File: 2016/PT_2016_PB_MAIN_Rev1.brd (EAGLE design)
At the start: 150.9 x 201.9 mm, 135 parts, among them Q1 Q_IRFS7437PbF, Q11 Q_IRFS7437PbF, Q12 2N7002, Q14 Q_IRFS7437PbF, Q16 Q_IRFS7437PbF, Q2 2N7002, Q20 Q_IRFS7437PbF, Q6 Q_IRFS7437PbF, Q7 Q_IRFS7437PbF, Q9 Q_IRFS7437PbF

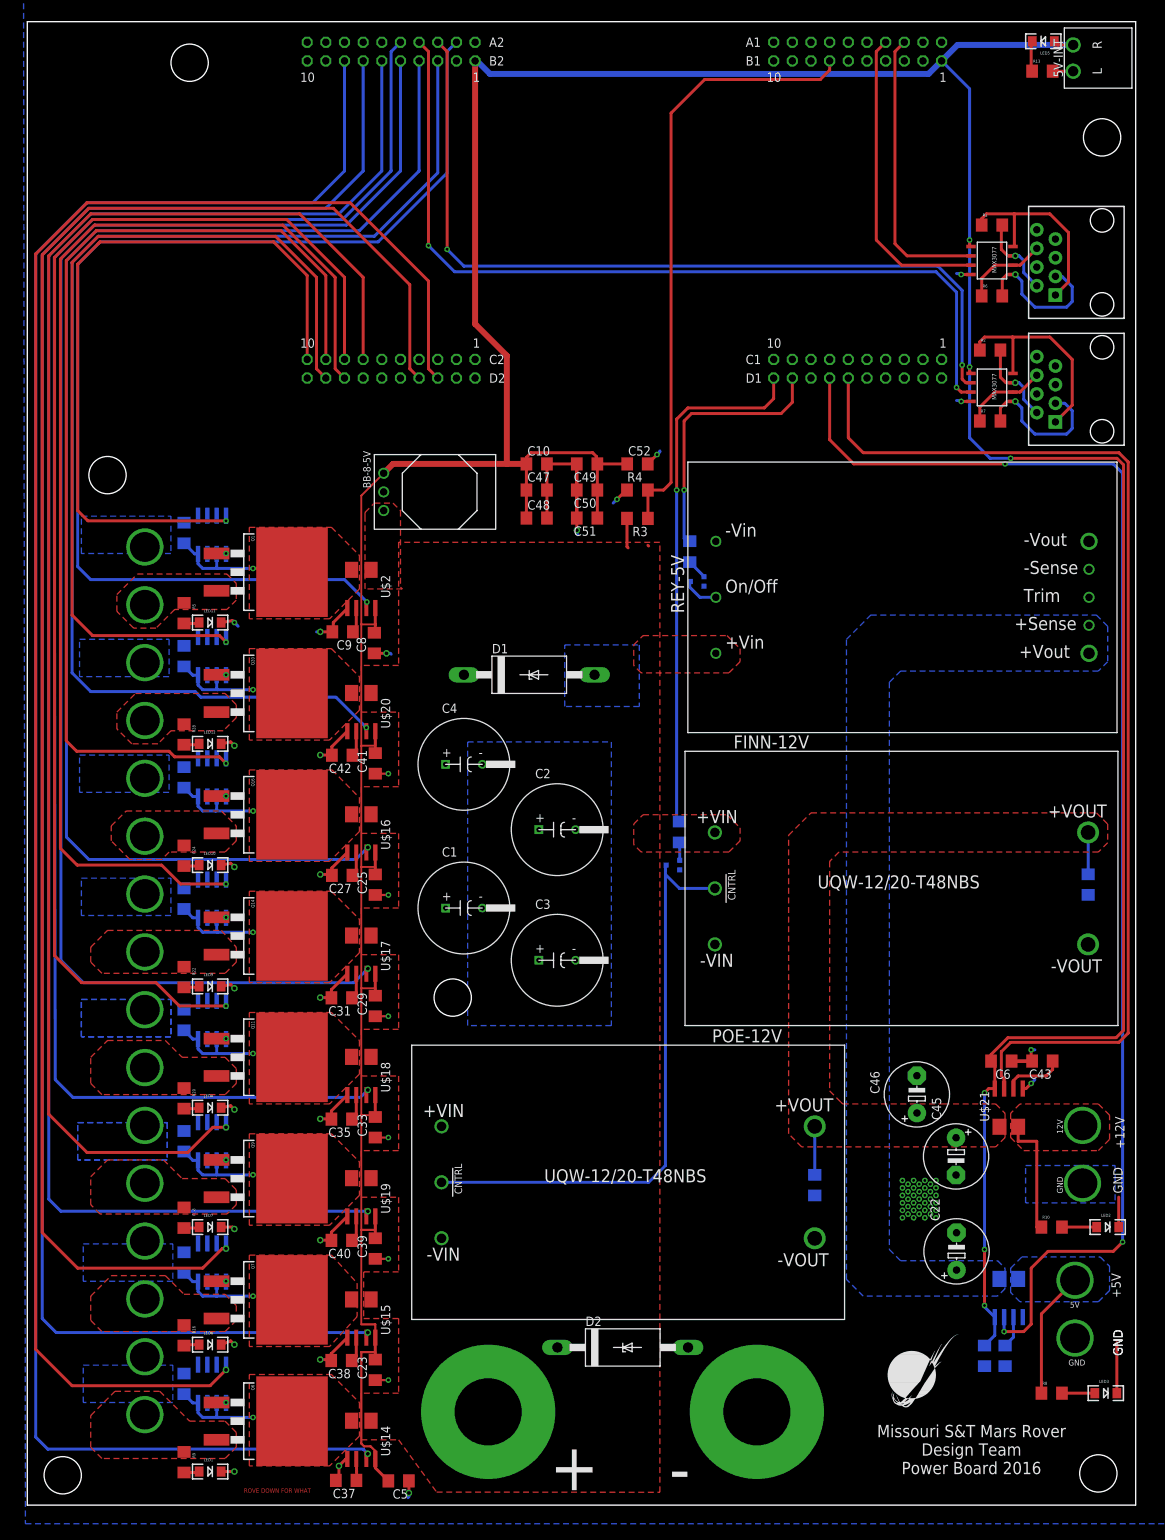
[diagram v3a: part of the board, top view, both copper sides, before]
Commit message: Added mounting wings for APP and rerouted
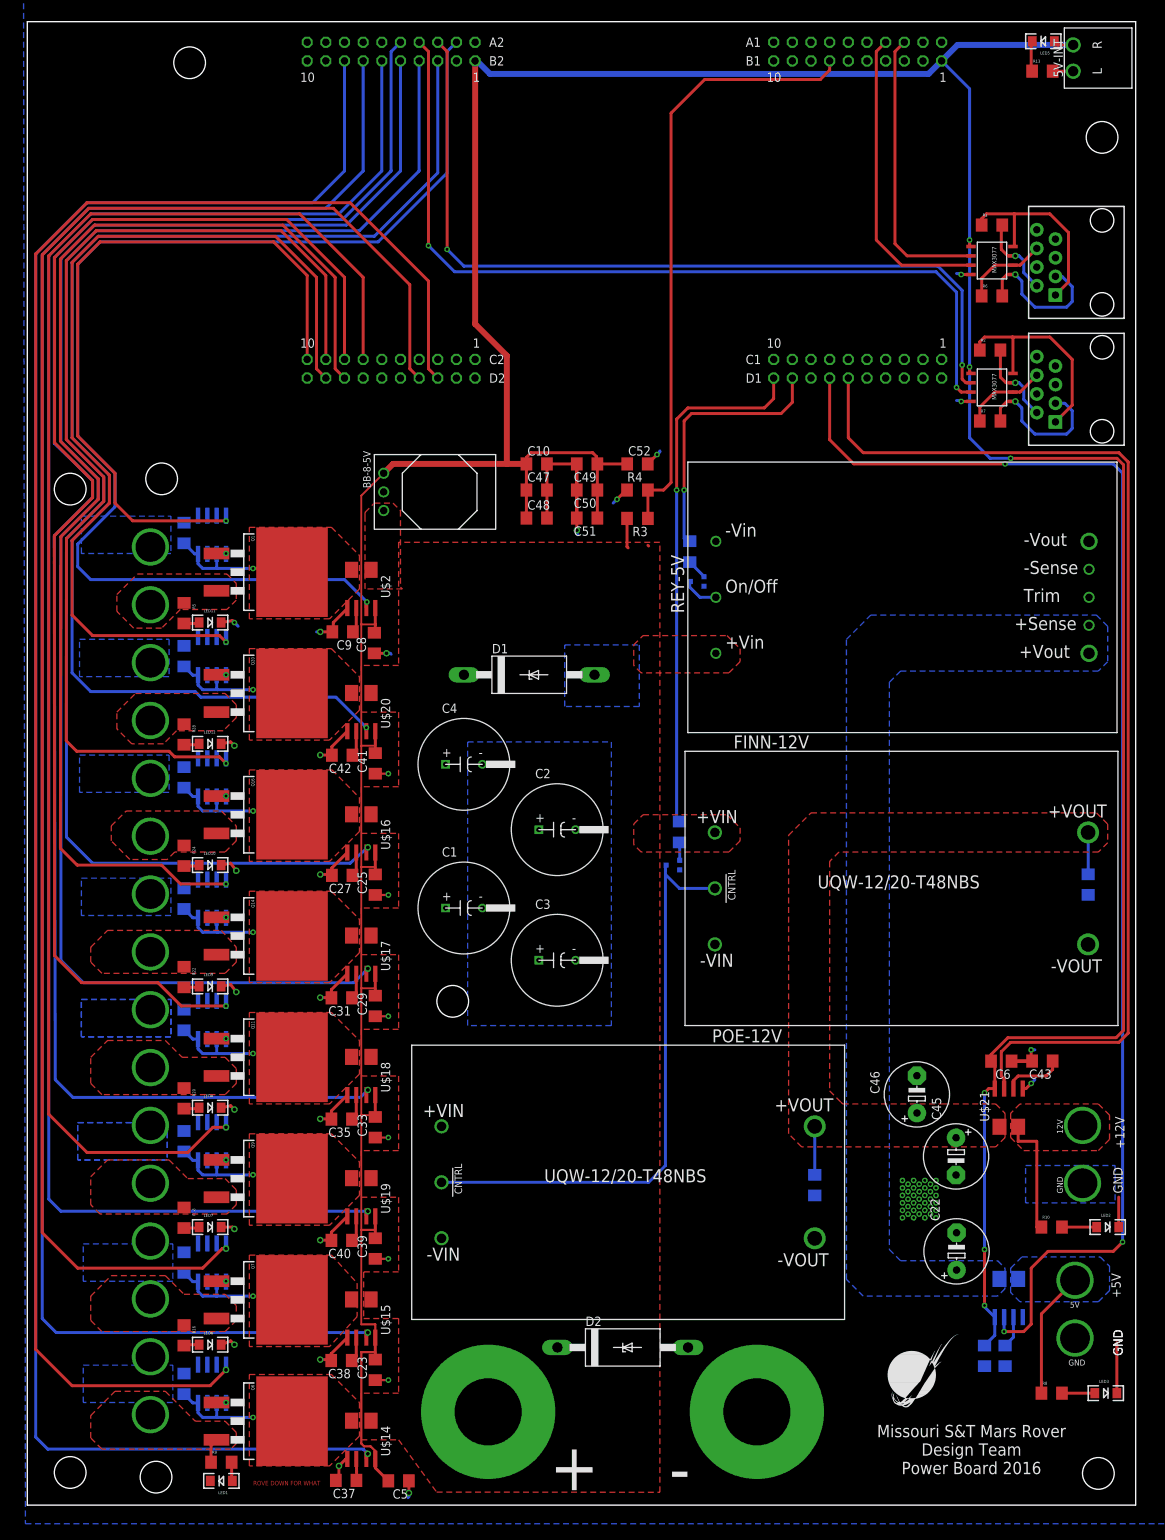
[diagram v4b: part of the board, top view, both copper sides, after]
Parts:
- added U$41, U$42: APP_MOUTING_WINGHORIZ, MRDT-Connectors:PP_MOUNTING_WING_HORIZ
- moved R9 5.08 mm to (21.6, 2.03), turned to 0 degrees
- moved LED1 1.98 mm to (21.6, -0.51), turned to 180 degrees
- moved U$25 0.76 mm to (-16.3, 75.4)
- moved U$26 0.76 mm to (-16.3, 114.8)
- moved U$27 0.76 mm to (-16.3, 43.9)
- moved U$28 0.76 mm to (-16.3, 67.6)
- moved U$29 0.76 mm to (-16.3, 106.9)
- moved U$30 0.76 mm to (-16.3, 99.1)
- moved U$31 0.76 mm to (-16.3, 122.7)
- moved U$32 0.76 mm to (-16.3, 36.1)
- moved U$33 0.76 mm to (-16.3, 91.2)
- moved U$34 0.76 mm to (-16.3, 51.8)
- moved U$35 0.76 mm to (-16.3, 12.4)
- moved U$36 0.76 mm to (-16.3, 83.3)
- moved U$37 0.76 mm to (-16.3, 59.7)
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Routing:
- net M6-IMEAS: track 191.2 -> 195.8 mm
- net M4-IMEAS: track 225.5 -> 229.8 mm
- net M4-SIG: track 177.9 -> 182.2 mm
- net M5-SIG: track 162.0 -> 166.2 mm
- net M6-SIG: track 140.1 -> 144.3 mm
- net AUX_P-IMEAS: track 169.6 -> 173.8 mm
- net M5-IMEAS: track 206.4 -> 210.6 mm
- net AUX_P2-IMEAS: track 157.2 -> 161.4 mm
- net AUX_P-SIG: track 122.5 -> 126.7 mm
- net AUX_P2-SIG: track 100.8 -> 97.3 mm
- net N$41: track 0.00 -> 3.36 mm
- net GND: track 136.9 -> 136.2 mm, vias 70 -> 69

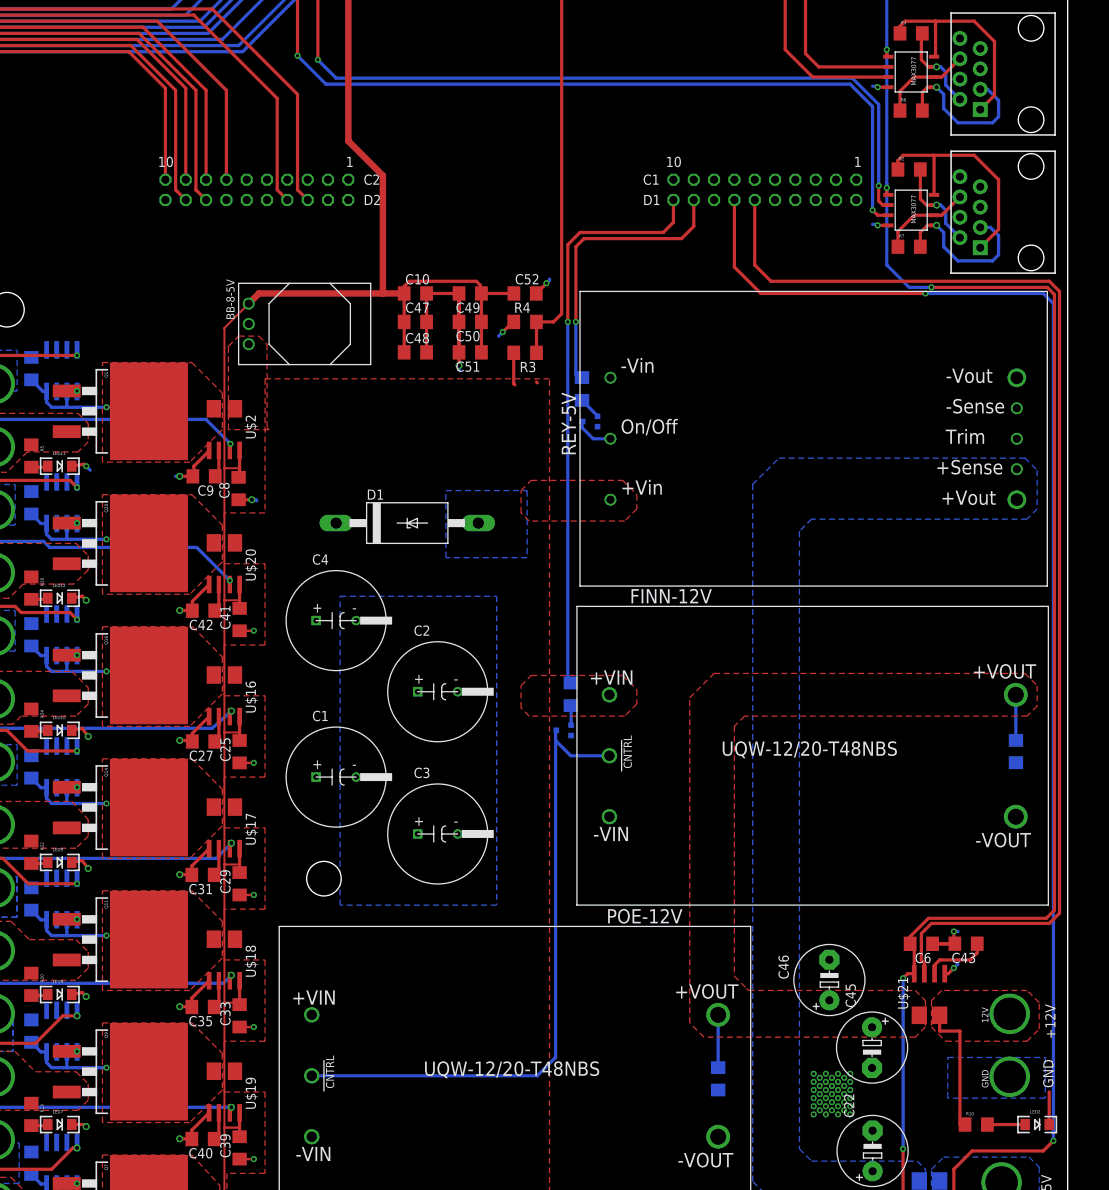
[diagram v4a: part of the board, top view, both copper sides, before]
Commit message: Fixed some clearance issues
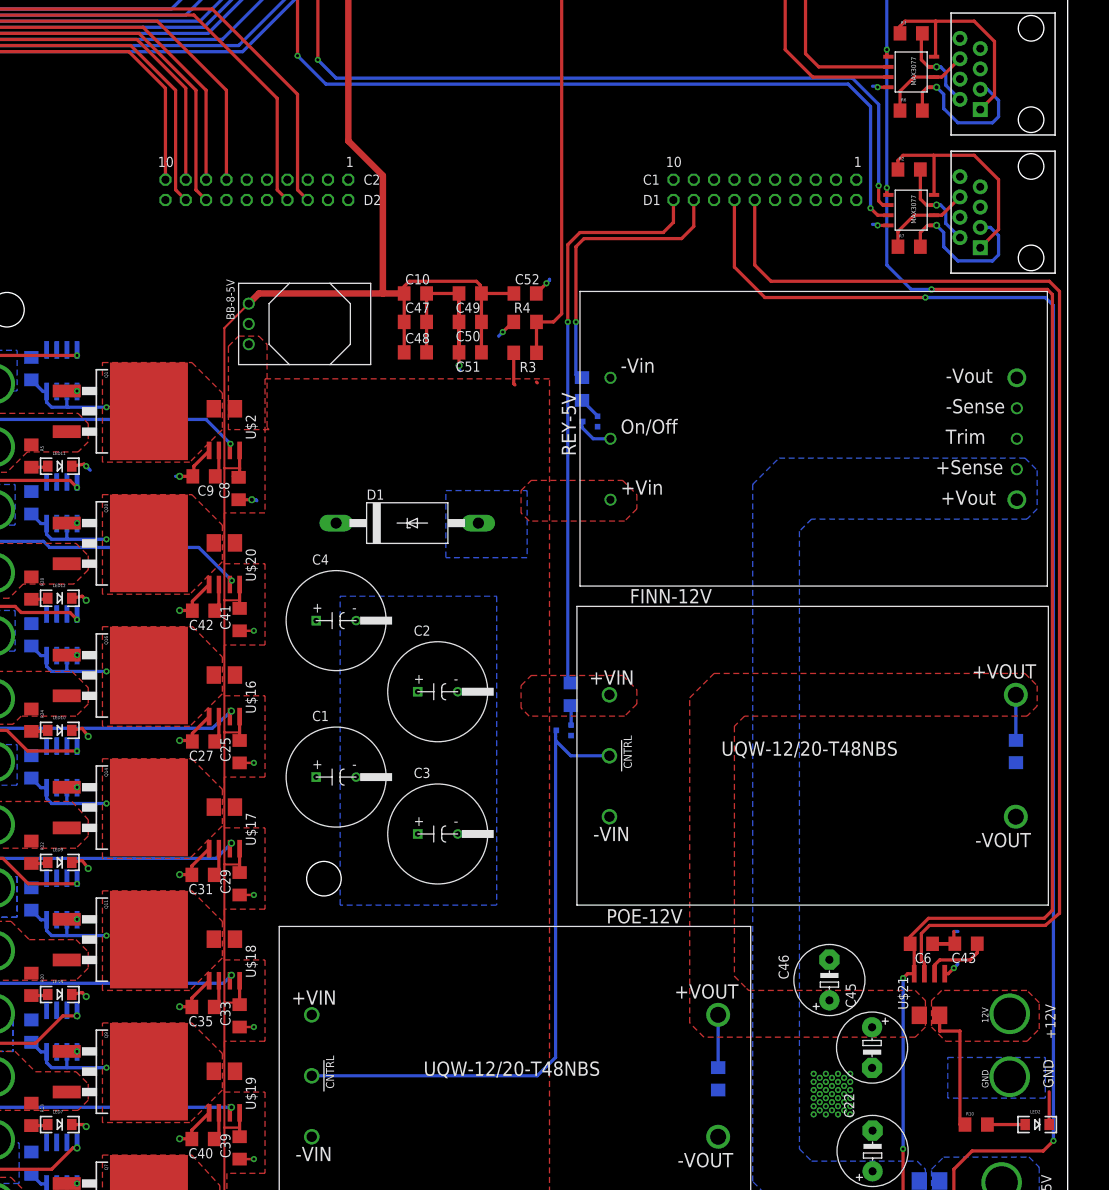
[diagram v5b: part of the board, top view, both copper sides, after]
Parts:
- renumbered U$25 to M5-, U$26 to AUX2+, U$27 to M3-, U$28 to M5+, U$29 to AUX1-, U$30 to AUX1+, U$31 to AUX2-, U$32 to M3+, U$33 to M6-, U$34 to M4+, U$35 to M1-, U$36 to M6+, U$37 to M4-, U$38 to M2+, U$39 to M2-, U$40 to M1+
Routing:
- net +5V: track 592.9 -> 592.4 mm
- net GND: vias 69 -> 68

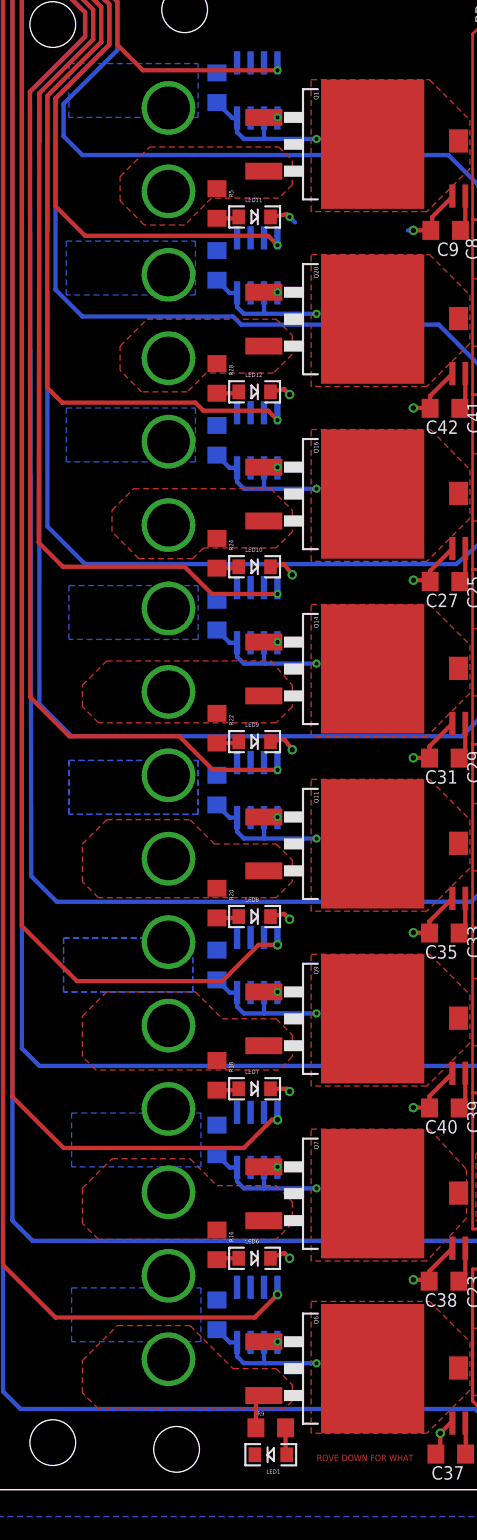
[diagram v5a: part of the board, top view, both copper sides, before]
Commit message: Deleted Unnecessary Polygons
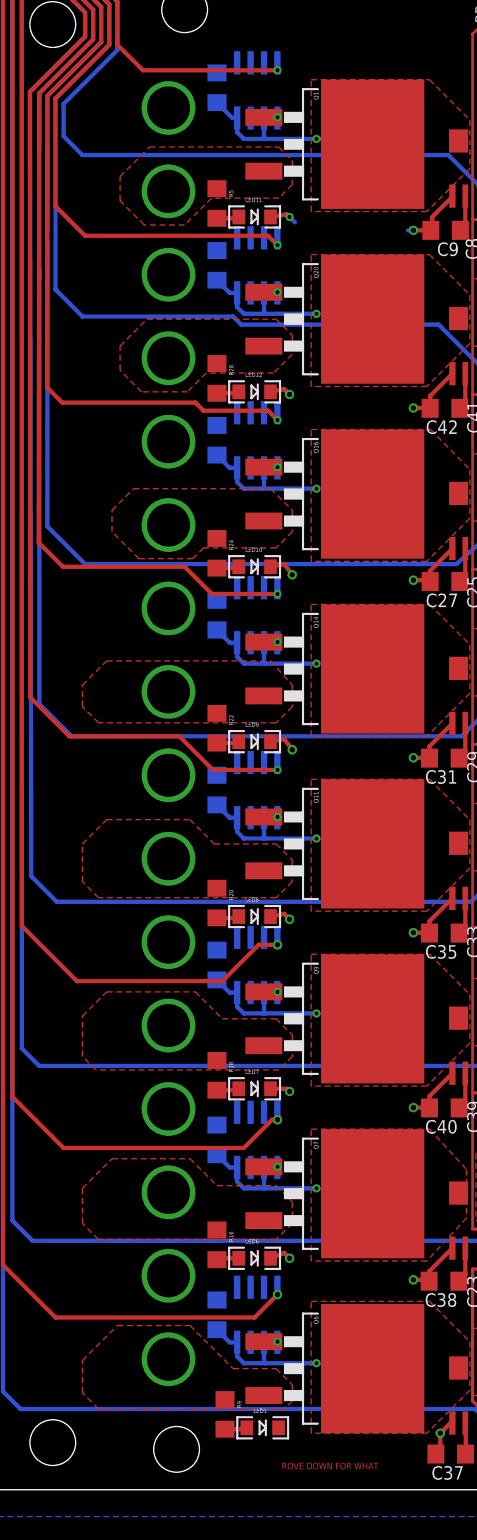
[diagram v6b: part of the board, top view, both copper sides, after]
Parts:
- moved R9 4.50 mm to (17.3, 3.30), turned to 270 degrees
- moved LED1 2.65 mm to (20.8, 2.03), turned to 0 degrees
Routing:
- net N$41: track 3.36 -> 0.00 mm
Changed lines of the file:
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@@
 <?xml version="1.0" encoding="utf-8"?>
 <!DOCTYPE eagle SYSTEM "eagle.dtd">
-<eagle version="6.5.0">
+<eagle version="7.1.0">
 <drawing>
 <settings>
@@
 <plain>
 <hole x="140.97" y="0.508" drill="4.318"/>
-<text x="35.052" y="-0.508" size="0.6096" layer="1" rot="R180">ROVE DOWN FOR WHAT</text>
+<text x="31.75" y="-1.27" size="0.6096" layer="1" rot="R180">ROVE DOWN FOR WHAT</text>
 <text x="123.698" y="7.112" size="1.6764" layer="21" rot="R180" align="bottom-center">Missouri S&amp;T Mars Rover
 Design Team
@@
 <pass name="Default">
 <param name="RoutingGrid" value="50mil"/>
+<param name="AutoGrid" value="1"/>
+<param name="Efforts" value="0"/>
+<param name="TopRouterVariant" value="1"/>
 <param name="tpViaShape" value="round"/>
 <param name="PrefDir.1" value="|"/>
@@
 <element name="U$6" library="Jake" package="SO8" value="LT1910" x="20.32" y="12.7" rot="MR180"/>
 <element name="C16" library="resistor" package="C1206" value="10µF" x="16.51" y="12.7" rot="MR270"/>
-<element name="LED1" library="SparkFun-LED" package="LED-1206" value="" x="21.59" y="-0.508" rot="R180"/>
-<element name="R9" library="SparkFun-Passives" package="1206" value="5kΩ" x="21.59" y="2.032"/>
+<element name="LED1" library="SparkFun-LED" package="LED-1206" value="" x="20.828" y="2.032"/>
+<element name="R9" library="SparkFun-Passives" package="1206" value="5kΩ" x="17.272" y="3.302" rot="R270"/>
 <element name="LED2" library="SparkFun-LED" package="LED-1206" value="" x="142.24" y="34.036"/>
 <element name="R10" library="SparkFun-Passives" package="1206" value="1kΩ" x="134.62" y="34.036"/>
@@
 </polygon>
 <polygon width="0.4064" layer="16" thermals="no">
-<vertex x="2.286" y="114.046"/>
-<vertex x="14.478" y="114.046"/>
-<vertex x="14.478" y="108.966"/>
-<vertex x="2.286" y="108.966"/>
-</polygon>
-<polygon width="0.4064" layer="16" thermals="no">
-<vertex x="2.286" y="98.298"/>
-<vertex x="14.478" y="98.298"/>
-<vertex x="14.478" y="93.218"/>
-<vertex x="2.286" y="93.218"/>
-</polygon>
-<polygon width="0.4064" layer="16" thermals="no">
-<vertex x="2.54" y="81.534"/>
-<vertex x="14.732" y="81.534"/>
-<vertex x="14.732" y="76.454"/>
-<vertex x="2.54" y="76.454"/>
-</polygon>
-<polygon width="0.4064" layer="16" thermals="no">
-<vertex x="2.54" y="65.024"/>
-<vertex x="14.732" y="65.024"/>
-<vertex x="14.732" y="59.944"/>
-<vertex x="2.54" y="59.944"/>
-</polygon>
-<polygon width="0.4064" layer="16" thermals="no">
-<vertex x="2.54" y="65.024"/>
-<vertex x="14.732" y="65.024"/>
-<vertex x="14.732" y="59.944"/>
-<vertex x="2.54" y="59.944"/>
-</polygon>
-<polygon width="0.4064" layer="16" thermals="no">
-<vertex x="2.032" y="48.26"/>
-<vertex x="14.224" y="48.26"/>
-<vertex x="14.224" y="43.18"/>
-<vertex x="2.032" y="43.18"/>
-</polygon>
-<polygon width="0.4064" layer="16" thermals="no">
-<vertex x="2.032" y="48.26"/>
-<vertex x="14.224" y="48.26"/>
-<vertex x="14.224" y="43.18"/>
-<vertex x="2.032" y="43.18"/>
-</polygon>
-<polygon width="0.4064" layer="16" thermals="no">
-<vertex x="2.794" y="31.75"/>
-<vertex x="14.986" y="31.75"/>
-<vertex x="14.986" y="26.67"/>
-<vertex x="2.794" y="26.67"/>
-</polygon>
-<polygon width="0.4064" layer="16" thermals="no">
-<vertex x="2.794" y="15.24"/>
-<vertex x="14.986" y="15.24"/>
-<vertex x="14.986" y="10.16"/>
-<vertex x="2.794" y="10.16"/>
-</polygon>
-<polygon width="0.4064" layer="16" thermals="no">
 <vertex x="68.326" y="113.284"/>
 <vertex x="78.486" y="113.284"/>
@@
 <contactref element="C9" pad="2"/>
 <contactref element="C8" pad="1"/>
-<polygon width="0.4064" layer="16" thermals="no">
-<vertex x="2.54" y="130.81"/>
-<vertex x="14.732" y="130.81"/>
-<vertex x="14.732" y="125.73"/>
-<vertex x="2.54" y="125.73"/>
-</polygon>
 <contactref element="U$12" pad="GND"/>
 <contactref element="U$5" pad="8"/>
@@
 </polygon>
 <contactref element="M1+" pad="P$1"/>
-<wire x1="20.19" y1="2.032" x2="20.19" y2="4.335" width="0.4064" layer="1"/>
-<wire x1="20.19" y1="4.335" x2="20.935" y2="5.08" width="0.4064" layer="1"/>
 </signal>
 <signal name="N$42">
@@
 <contactref element="R9" pad="2"/>
 <contactref element="LED1" pad="A"/>
-<wire x1="22.99" y1="2.032" x2="22.99" y2="-0.408" width="0.4064" layer="1"/>
-<wire x1="22.99" y1="-0.408" x2="23.09" y2="-0.508" width="0.4064" layer="1"/>
+<wire x1="17.272" y1="1.902" x2="19.328" y2="1.902" width="0.4064" layer="1"/>
+<wire x1="19.328" y1="1.902" x2="19.328" y2="2.032" width="0.4064" layer="1"/>
 </signal>
 <signal name="N$46">
